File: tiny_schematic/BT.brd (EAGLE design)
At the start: 160 x 100 mm, 2 parts

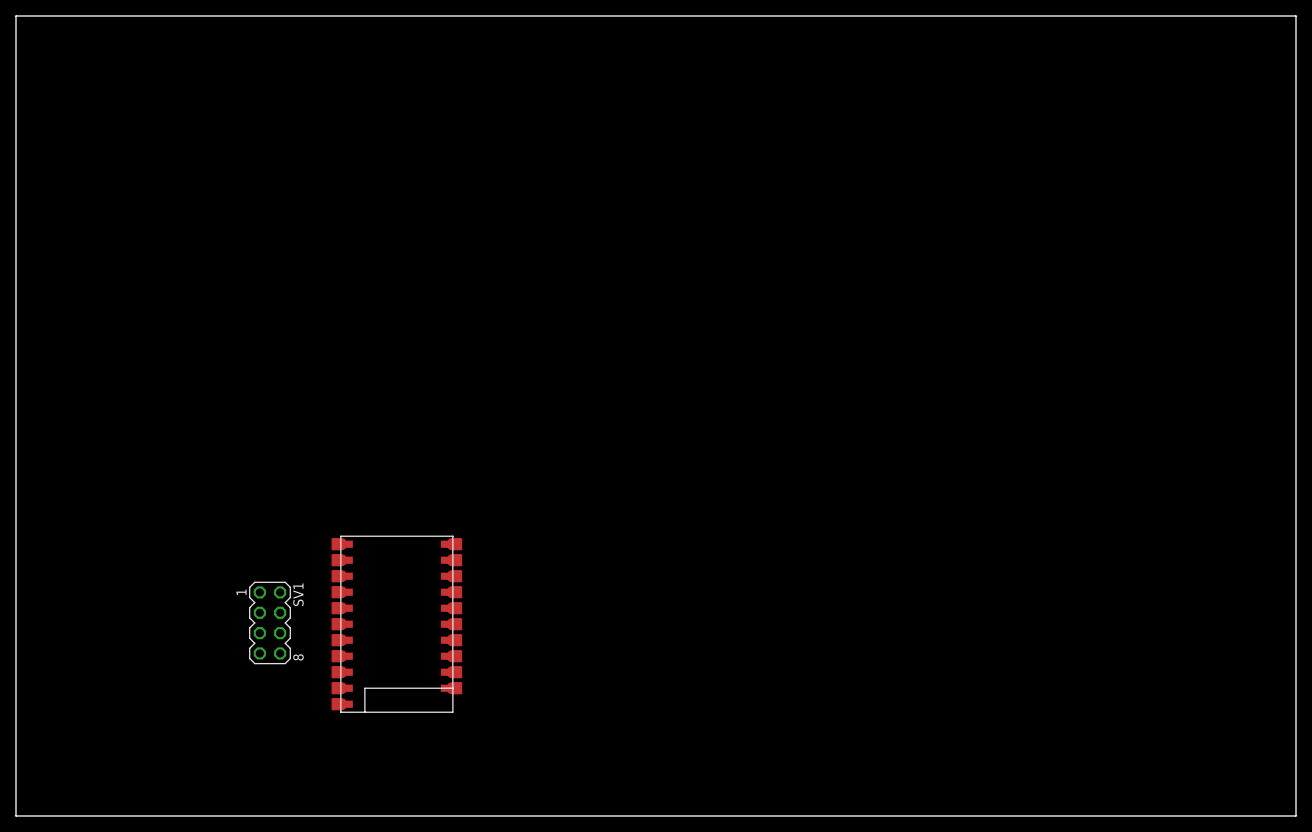
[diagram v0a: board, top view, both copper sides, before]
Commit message: BT-Module finished IR-header moved
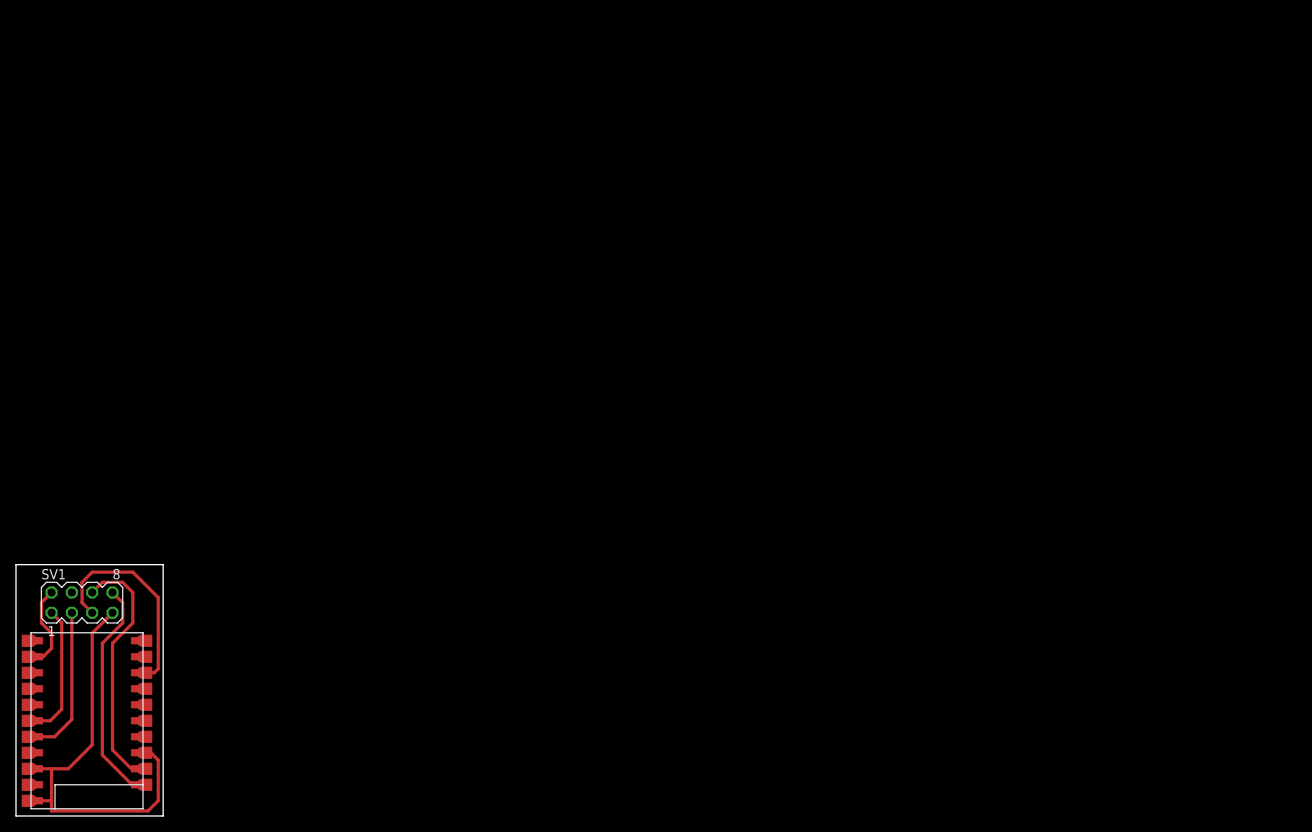
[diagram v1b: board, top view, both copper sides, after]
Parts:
- moved BT1 40.6 mm to (15.9, 1.91)
- moved SV1 23.6 mm to (8.26, 26.7), turned to 0 degrees
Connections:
- new net N$9: SV1.4
- net N$3: now also SV1.6; no longer SV1.5
- net N$6: now also SV1.5; no longer SV1.6
- net N$7: no longer SV1.4
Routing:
- net N$4: track 0.00 -> 55.3 mm
- net N$3: track 0.00 -> 31.6 mm
- net N$5: track 0.00 -> 28.3 mm
- net N$6: track 0.00 -> 26.9 mm
- net N$1: track 0.00 -> 19.1 mm
- net N$2: track 0.00 -> 16.8 mm
- net N$8: track 0.00 -> 10.8 mm
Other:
- board size 160 x 100 mm -> 18.4 x 31.4 mm
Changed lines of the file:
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@@
 <setting verticaltext="up"/>
 </settings>
-<grid distance="0.05" unitdist="inch" unit="inch" style="lines" multiple="1" display="no" altdistance="0.025" altunitdist="inch" altunit="inch"/>
+<grid distance="25" unitdist="mil" unit="mil" style="lines" multiple="1" display="no" altdistance="0.025" altunitdist="inch" altunit="inch"/>
 <layers>
 <layer number="1" name="Top" color="4" fill="1" visible="yes" active="yes"/>
@@
 <board>
 <plain>
-<wire x1="0" y1="0" x2="160" y2="0" width="0" layer="20"/>
-<wire x1="160" y1="0" x2="160" y2="100" width="0" layer="20"/>
-<wire x1="160" y1="100" x2="0" y2="100" width="0" layer="20"/>
-<wire x1="0" y1="100" x2="0" y2="0" width="0" layer="20"/>
+<wire x1="0" y1="0" x2="18.395" y2="0" width="0" layer="20"/>
+<wire x1="18.395" y1="0" x2="18.395" y2="31.42" width="0" layer="20"/>
+<wire x1="18.395" y1="31.42" x2="0" y2="31.42" width="0" layer="20"/>
+<wire x1="0" y1="31.42" x2="0" y2="0" width="0" layer="20"/>
 </plain>
 <attributes>
@@
 </autorouter>
 <elements>
-<element name="SV1" library="con-lstb" package="MA04-2" value="" x="31.75" y="24.13" rot="R270">
-<attribute name="OC_NEWARK" value="unknown" x="3.81" y="5.08" size="1.778" layer="27" rot="R270" display="off"/>
-<attribute name="MPN" value="" x="3.81" y="5.08" size="1.778" layer="27" rot="R270" display="off"/>
-<attribute name="MF" value="" x="3.81" y="5.08" size="1.778" layer="27" rot="R270" display="off"/>
-<attribute name="OC_FARNELL" value="unknown" x="3.81" y="5.08" size="1.778" layer="27" rot="R270" display="off"/>
+<element name="SV1" library="con-lstb" package="MA04-2" value="" x="8.255" y="26.67">
+<attribute name="OC_NEWARK" value="unknown" x="27.305" y="-1.27" size="1.778" layer="27" display="off"/>
+<attribute name="MPN" value="" x="27.305" y="-1.27" size="1.778" layer="27" display="off"/>
+<attribute name="MF" value="" x="27.305" y="-1.27" size="1.778" layer="27" display="off"/>
+<attribute name="OC_FARNELL" value="unknown" x="27.305" y="-1.27" size="1.778" layer="27" display="off"/>
 </element>
-<element name="BT1" library="tinyLight" package="BT_MODULE" value="ARDEUNIS_BT_787" x="54.61" y="13.97" rot="R180"/>
+<element name="BT1" library="tinyLight" package="BT_MODULE" value="ARDEUNIS_BT_787" x="15.875" y="1.905" rot="R180"/>
 </elements>
 <signals>
@@
 <contactref element="BT1" pad="P15"/>
 <contactref element="SV1" pad="3"/>
-<wire x1="30.48" y1="25.4" x2="40.81" y2="21.97" width="0" layer="19" extent="1-1"/>
+<wire x1="6.985" y1="25.4" x2="6.985" y2="12.065" width="0.4064" layer="1"/>
+<wire x1="6.985" y1="12.065" x2="4.825" y2="9.905" width="0.4064" layer="1"/>
+<wire x1="4.825" y1="9.905" x2="2.075" y2="9.905" width="0.4064" layer="1"/>
 </signal>
 <signal name="N$2">
 <contactref element="SV1" pad="1"/>
 <contactref element="BT1" pad="P16"/>
-<wire x1="30.48" y1="27.94" x2="40.81" y2="23.97" width="0" layer="19" extent="1-1"/>
+<wire x1="4.445" y1="25.4" x2="5.715" y2="24.13" width="0.4064" layer="1"/>
+<wire x1="5.715" y1="24.13" x2="5.715" y2="13.335" width="0.4064" layer="1"/>
+<wire x1="2.075" y1="11.905" x2="4.285" y2="11.905" width="0.4064" layer="1"/>
+<wire x1="4.285" y1="11.905" x2="5.715" y2="13.335" width="0.4064" layer="1"/>
 </signal>
 <signal name="N$3">
-<contactref element="SV1" pad="5"/>
 <contactref element="BT1" pad="P2"/>
-<wire x1="30.48" y1="22.86" x2="54.41" y2="17.97" width="0" layer="19" extent="1-1"/>
+<contactref element="SV1" pad="6"/>
+<wire x1="9.525" y1="27.94" x2="10.795" y2="29.21" width="0.4064" layer="1"/>
+<wire x1="10.795" y1="29.21" x2="13.335" y2="29.21" width="0.4064" layer="1"/>
+<wire x1="13.335" y1="29.21" x2="14.605" y2="27.94" width="0.4064" layer="1"/>
+<wire x1="14.605" y1="27.94" x2="14.605" y2="24.13" width="0.4064" layer="1"/>
+<wire x1="14.605" y1="24.13" x2="12.065" y2="21.59" width="0.4064" layer="1"/>
+<wire x1="12.065" y1="21.59" x2="12.065" y2="8.255" width="0.4064" layer="1"/>
+<wire x1="12.065" y1="8.255" x2="14.605" y2="5.715" width="0.4064" layer="1"/>
+<wire x1="14.605" y1="5.715" x2="15.485" y2="5.715" width="0.4064" layer="1"/>
+<wire x1="15.485" y1="5.715" x2="15.675" y2="5.905" width="0.4064" layer="1"/>
 </signal>
 <signal name="N$4">
@@
 <contactref element="BT1" pad="P11"/>
 <contactref element="BT1" pad="P13"/>
-<wire x1="40.81" y1="17.97" x2="54.41" y2="19.97" width="0" layer="19" extent="1-1"/>
-<wire x1="40.81" y1="13.97" x2="40.81" y2="17.97" width="0" layer="19" extent="1-1"/>
-<wire x1="30.48" y1="20.32" x2="40.81" y2="17.97" width="0" layer="19" extent="1-1"/>
+<wire x1="12.065" y1="25.4" x2="9.525" y2="22.86" width="0.4064" layer="1"/>
+<wire x1="9.525" y1="22.86" x2="9.525" y2="8.89" width="0.4064" layer="1"/>
+<wire x1="9.525" y1="8.89" x2="6.54" y2="5.905" width="0.4064" layer="1"/>
+<wire x1="6.54" y1="5.905" x2="4.445" y2="5.905" width="0.4064" layer="1"/>
+<wire x1="4.445" y1="5.905" x2="2.075" y2="5.905" width="0.4064" layer="1"/>
+<wire x1="2.075" y1="1.905" x2="4.445" y2="1.905" width="0.4064" layer="1"/>
+<wire x1="4.445" y1="1.905" x2="4.445" y2="5.905" width="0.4064" layer="1"/>
+<wire x1="17.78" y1="0.635" x2="16.51" y2="0.635" width="0" layer="19" extent="1-16"/>
+<wire x1="16.51" y1="0.635" x2="4.445" y2="0.635" width="0.4064" layer="1"/>
+<wire x1="4.445" y1="0.635" x2="4.445" y2="1.905" width="0.4064" layer="1"/>
+<wire x1="15.675" y1="7.905" x2="16.86" y2="7.905" width="0.4064" layer="1"/>
+<wire x1="16.86" y1="7.905" x2="17.78" y2="6.985" width="0.4064" layer="1"/>
+<wire x1="17.78" y1="6.985" x2="17.78" y2="1.905" width="0.4064" layer="1"/>
+<wire x1="17.78" y1="1.905" x2="16.51" y2="0.635" width="0.4064" layer="1"/>
 </signal>
 <signal name="N$5">
 <contactref element="SV1" pad="8"/>
 <contactref element="BT1" pad="P1"/>
-<wire x1="33.02" y1="20.32" x2="54.41" y2="15.97" width="0" layer="19" extent="1-1"/>
+<wire x1="12.065" y1="27.94" x2="13.335" y2="26.67" width="0.4064" layer="1"/>
+<wire x1="13.335" y1="26.67" x2="13.335" y2="24.13" width="0.4064" layer="1"/>
+<wire x1="13.335" y1="24.13" x2="10.795" y2="21.59" width="0.4064" layer="1"/>
+<wire x1="10.795" y1="21.59" x2="10.795" y2="7.62" width="0.4064" layer="1"/>
+<wire x1="10.795" y1="7.62" x2="14.51" y2="3.905" width="0.4064" layer="1"/>
+<wire x1="14.51" y1="3.905" x2="15.675" y2="3.905" width="0.4064" layer="1"/>
+</signal>
+<signal name="N$7">
+<contactref element="BT1" pad="P19"/>
+</signal>
+<signal name="N$8">
+<contactref element="BT1" pad="P20"/>
+<contactref element="SV1" pad="2"/>
+<wire x1="4.445" y1="22.86" x2="4.445" y2="20.955" width="0.4064" layer="1"/>
+<wire x1="4.445" y1="27.94" x2="3.175" y2="26.67" width="0.4064" layer="1"/>
+<wire x1="3.175" y1="26.67" x2="3.175" y2="24.13" width="0.4064" layer="1"/>
+<wire x1="3.175" y1="24.13" x2="4.445" y2="22.86" width="0.4064" layer="1"/>
+<wire x1="4.445" y1="20.955" x2="3.395" y2="19.905" width="0.4064" layer="1"/>
+<wire x1="3.395" y1="19.905" x2="2.075" y2="19.905" width="0.4064" layer="1"/>
 </signal>
 <signal name="N$6">
-<contactref element="SV1" pad="6"/>
+<contactref element="SV1" pad="5"/>
 <contactref element="BT1" pad="P8"/>
-<wire x1="33.02" y1="22.86" x2="54.41" y2="29.97" width="0" layer="19" extent="1-1"/>
-</signal>
-<signal name="N$7">
+<wire x1="9.525" y1="25.4" x2="8.255" y2="26.67" width="0.4064" layer="1"/>
+<wire x1="8.255" y1="26.67" x2="8.255" y2="29.21" width="0.4064" layer="1"/>
+<wire x1="8.255" y1="29.21" x2="9.525" y2="30.48" width="0.4064" layer="1"/>
+<wire x1="9.525" y1="30.48" x2="14.605" y2="30.48" width="0.4064" layer="1"/>
+<wire x1="14.605" y1="30.48" x2="17.78" y2="27.305" width="0.4064" layer="1"/>
+<wire x1="17.78" y1="27.305" x2="17.78" y2="18.415" width="0.4064" layer="1"/>
+<wire x1="15.675" y1="17.905" x2="17.27" y2="17.905" width="0.4064" layer="1"/>
+<wire x1="17.27" y1="17.905" x2="17.78" y2="18.415" width="0.4064" layer="1"/>
+</signal>
+<signal name="N$9">
 <contactref element="SV1" pad="4"/>
-<contactref element="BT1" pad="P19"/>
-<wire x1="33.02" y1="25.4" x2="40.81" y2="29.97" width="0" layer="19" extent="1-1"/>
-</signal>
-<signal name="N$8">
-<contactref element="SV1" pad="2"/>
-<contactref element="BT1" pad="P20"/>
-<wire x1="33.02" y1="27.94" x2="40.81" y2="31.97" width="0" layer="19" extent="1-1"/>
 </signal>
 </signals>

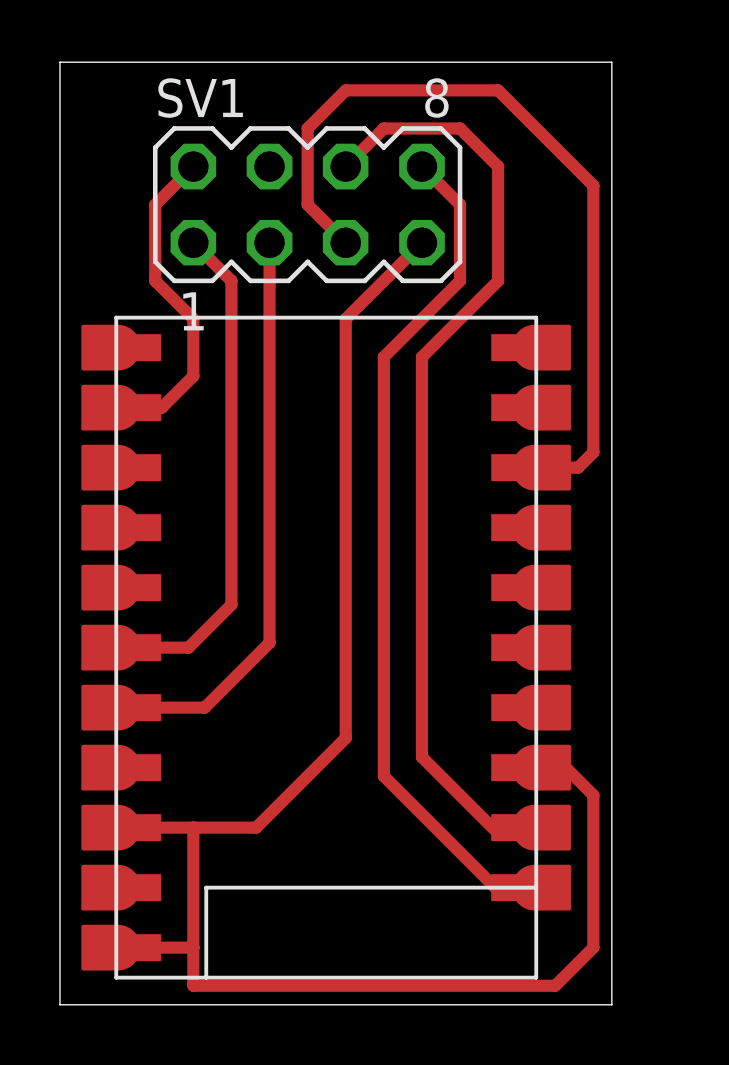
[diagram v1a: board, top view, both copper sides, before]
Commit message: BT implemented
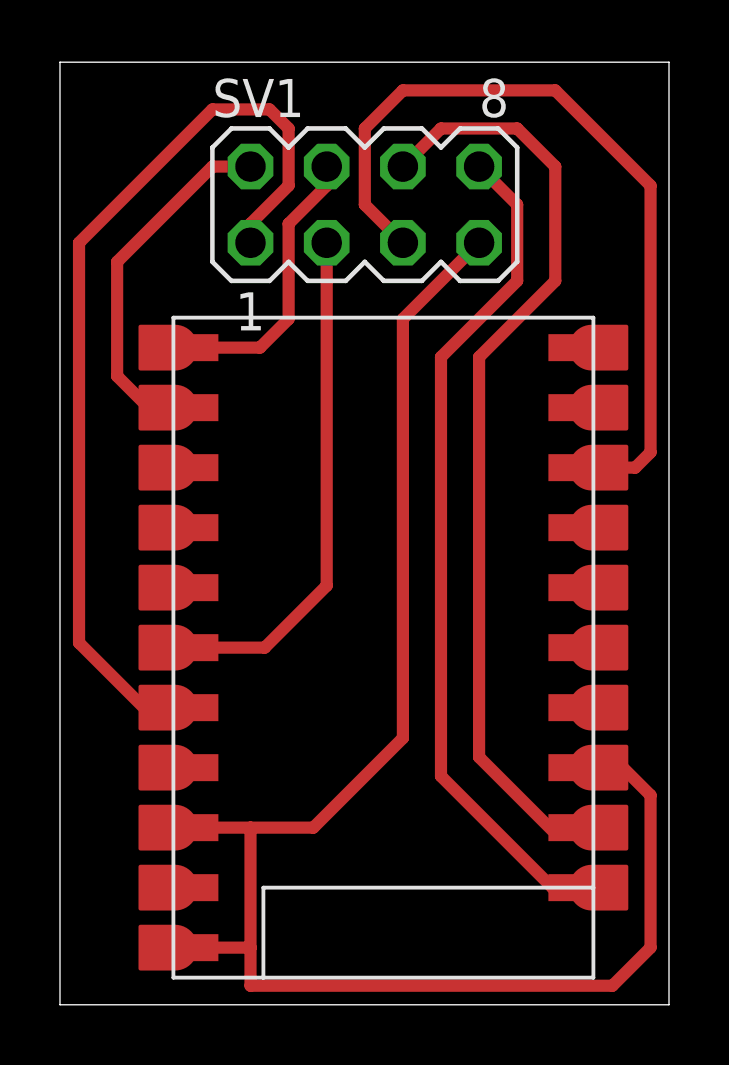
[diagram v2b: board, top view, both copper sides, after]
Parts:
- moved BT1 1.91 mm to (17.8, 1.91)
- moved SV1 1.90 mm to (10.2, 26.7)
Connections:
- removed net N$9: SV1.4
- net N$1: now also BT1.P16; no longer BT1.P15
- net N$2: now also BT1.P15; no longer BT1.P16
- net N$7: now also BT1.P21, SV1.4; no longer BT1.P19
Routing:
- net N$2: track 16.8 -> 31.3 mm
- net N$7: track 0.00 -> 9.64 mm
- net N$1: track 19.1 -> 17.2 mm
- net N$8: track 10.8 -> 12.3 mm
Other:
- board size 18.4 x 31.4 mm -> 20.3 x 31.4 mm

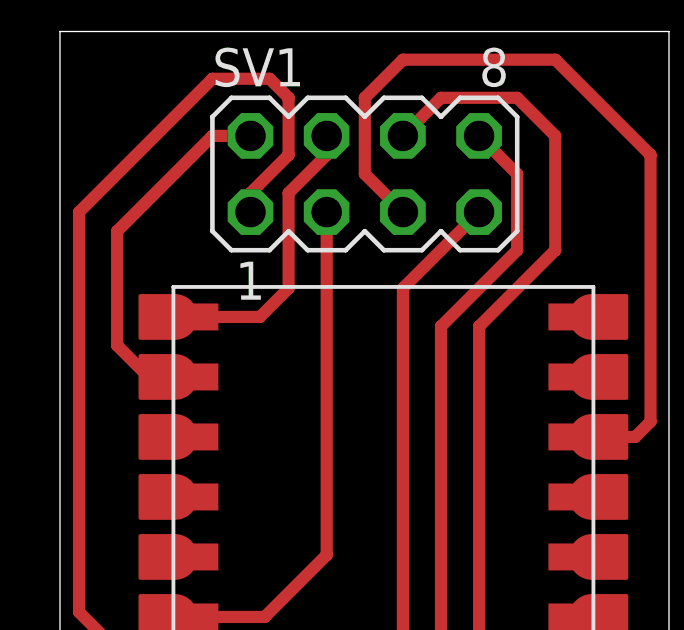
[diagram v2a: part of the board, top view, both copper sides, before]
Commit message: BT-layout changed, sleeping status value implemented, IR-alpha implemented
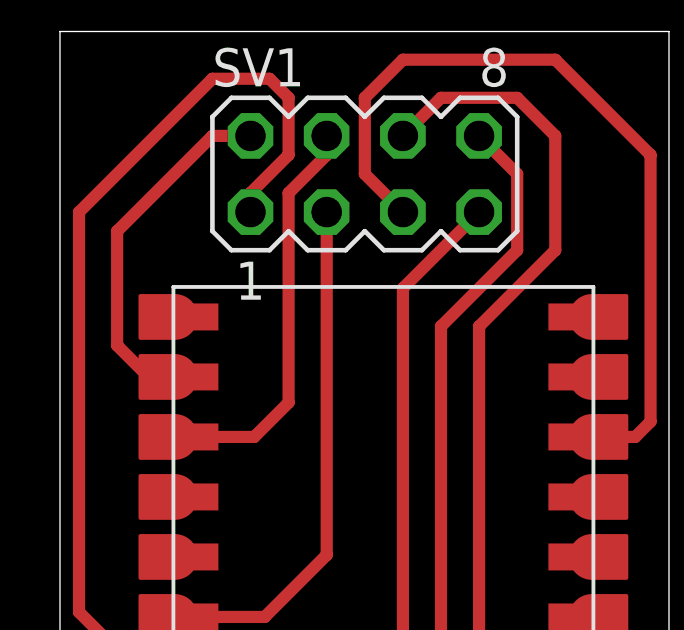
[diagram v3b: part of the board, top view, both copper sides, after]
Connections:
- net N$7: now also BT1.P19; no longer BT1.P21
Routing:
- net N$7: track 9.64 -> 13.5 mm
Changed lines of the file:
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@@
 </signal>
 <signal name="N$7">
-<contactref element="BT1" pad="P21"/>
 <contactref element="SV1" pad="4"/>
-<wire x1="3.98" y1="21.905" x2="6.665" y2="21.905" width="0.4064" layer="1"/>
-<wire x1="6.665" y1="21.905" x2="7.62" y2="22.86" width="0.4064" layer="1"/>
-<wire x1="7.62" y1="22.86" x2="7.62" y2="26.035" width="0.4064" layer="1"/>
 <wire x1="7.62" y1="26.035" x2="8.89" y2="27.305" width="0.4064" layer="1"/>
 <wire x1="8.89" y1="27.305" x2="8.89" y2="27.94" width="0.4064" layer="1"/>
+<contactref element="BT1" pad="P19"/>
+<wire x1="3.98" y1="17.905" x2="6.475" y2="17.905" width="0.4064" layer="1"/>
+<wire x1="6.475" y1="17.905" x2="7.62" y2="19.05" width="0.4064" layer="1"/>
+<wire x1="7.62" y1="19.05" x2="7.62" y2="26.035" width="0.4064" layer="1"/>
 </signal>
 </signals>
